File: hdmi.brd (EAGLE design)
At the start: 160 x 100 mm, 151 parts, among them IC1 FT2232HQ, U0 6SLX45CSG324, U1 MT41J64M16, U2 TPD12S016RKTR, U3 TPD12S016RKTR, U4 TPD12S016RKTR, U5 MNR18, U6 MNR18, U8 20Mhz

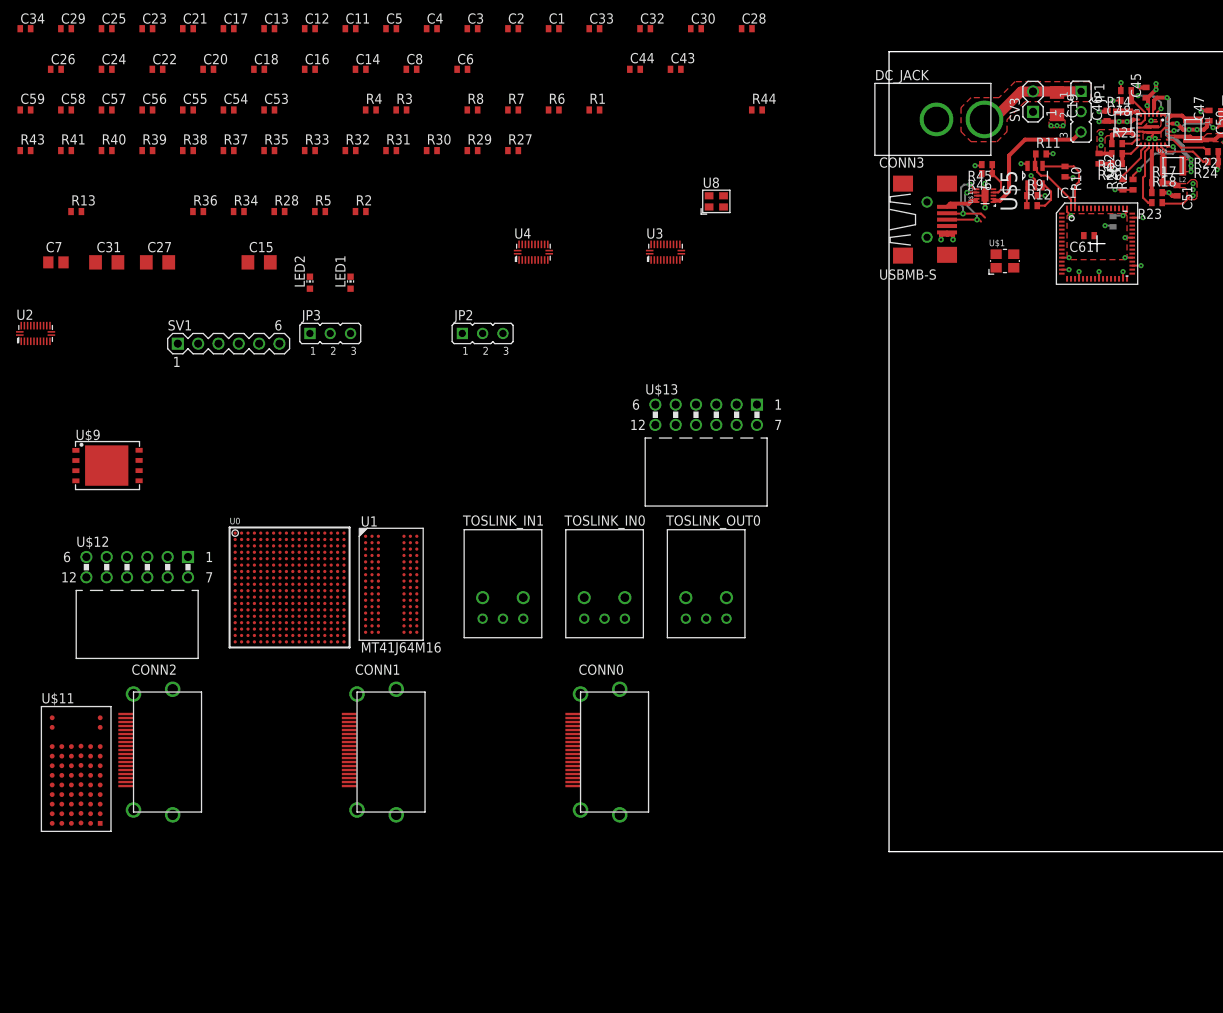
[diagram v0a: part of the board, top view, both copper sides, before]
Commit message: Rerouted USB, added more bypass capacitors at the FT2232H
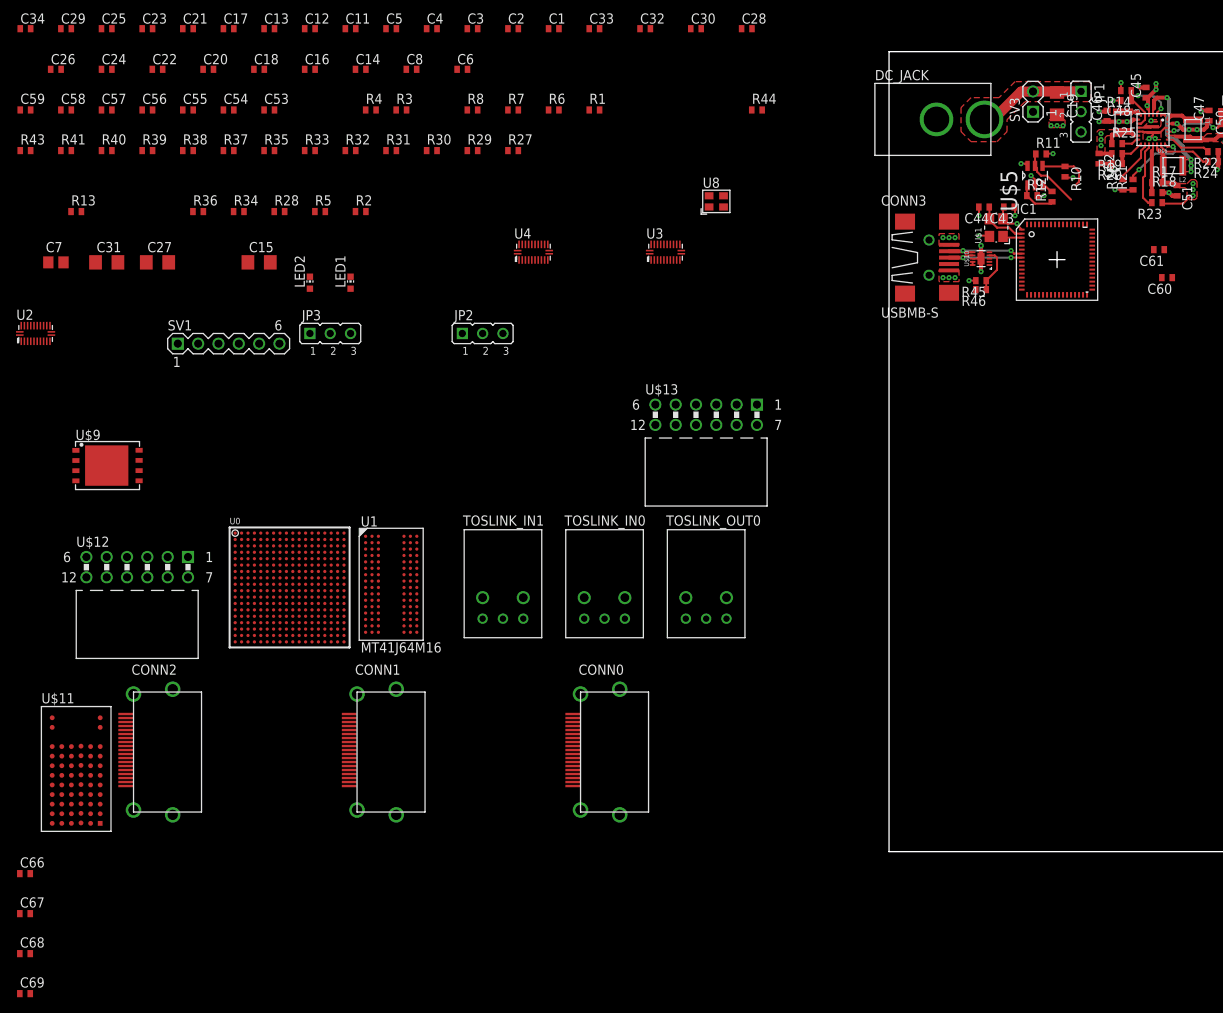
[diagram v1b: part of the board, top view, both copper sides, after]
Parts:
- added C66, C67, C68, C69: 0.1u, resistor:C0402
- C60: value 0.1u -> 4.7u
- moved C44 46.9 mm to (11.9, 80.6), turned to 180 degrees
- moved C43 45.1 mm to (15.0, 80.6), turned to 180 degrees
- moved R45 14.5 mm to (11.5, 71.4)
- moved R46 14.5 mm to (11.5, 70.2)
- moved C60 9.72 mm to (34.8, 71.8), flipped to the top, turned to 180 degrees
- moved C61 8.92 mm to (33.8, 75.2)
- moved U$10 7.89 mm to (11.5, 74.1)
- moved IC1 5.39 mm to (21.0, 74.0)
- moved CONN3 4.76 mm to (5.00, 74.2)
- moved U$1 4.35 mm to (13.4, 78.0), turned to 90 degrees
- moved R12 2.74 mm to (20.4, 81.9), turned to 90 degrees
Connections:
- net +1V8: now also C66.1, C67.1
- net +3V3: now also C68.1, C69.1
- net GND: now also C66.2, C67.2, C68.2, C69.2
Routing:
- net USB_VBUS: track 17.6 -> 0.00 mm
- net N$1: track 0.00 -> 6.39 mm
- net +1V8: track 5.31 -> 0.00 mm, vias 4 -> 0
- net N$45: track 4.51 -> 0.40 mm, vias 0 -> 3
- net N$5: track 0.00 -> 3.53 mm, vias 0 -> 1
- net N$10: track 4.42 -> 1.50 mm
- net +3V3: track 18.4 -> 15.5 mm, vias 12 -> 9
- net N$9: track 9.67 -> 6.82 mm
- net N$12: track 2.57 -> 5.03 mm
- net GND: track 36.7 -> 35.5 mm, vias 23 -> 22
- net N$6: track 9.15 -> 8.05 mm
- net USB_5V_ACK#: track 4.68 -> 5.62 mm
- net N$8: track 9.66 -> 10.4 mm
- added copper zone on layer 1, net N$45
- removed copper zone on layer 1, net +1V8

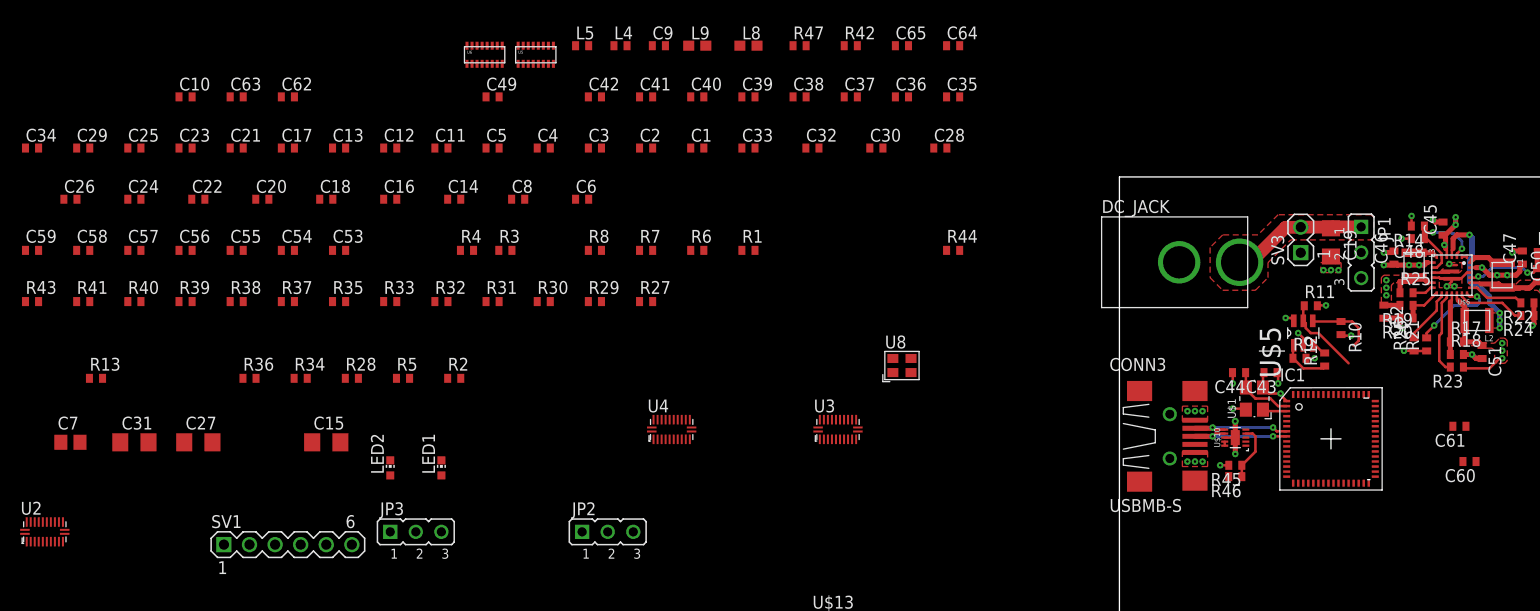
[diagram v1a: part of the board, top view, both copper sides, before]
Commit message: More USB related routing
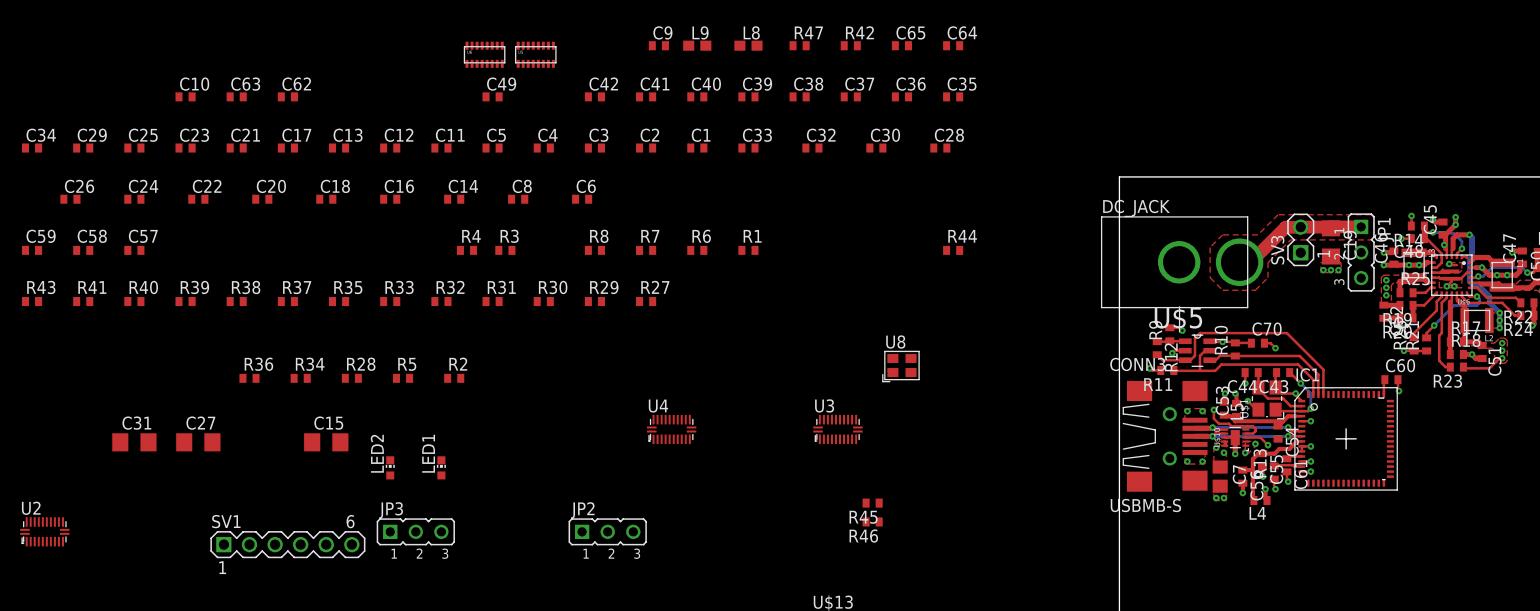
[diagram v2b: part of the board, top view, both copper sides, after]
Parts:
- added C70: 0.1u, resistor:C0402
- C53: value 0.1u -> 4.7u
- C54: value 4.7u -> 0.1u
- moved R13 117.3 mm to (15.4, 70.7), turned to 90 degrees
- moved C7 114.2 mm to (10.0, 70.2), turned to 270 degrees
- moved C56 107.3 mm to (12.2, 70.2), turned to 270 degrees
- moved C55 103.9 mm to (14.2, 71.9), turned to 270 degrees
- moved C54 99.9 mm to (15.8, 74.6), turned to 270 degrees
- moved C53 90.5 mm to (11.6, 76.9), turned to 90 degrees
- moved L4 77.9 mm to (14.0, 67.9), turned to 180 degrees
- moved L5 73.2 mm to (10.4, 77.0), turned to 270 degrees
- moved R46 36.3 mm to (-24.5, 65.8)
- moved R45 36.2 mm to (-24.5, 67.6)
- moved C61 17.6 mm to (16.6, 71.4), turned to 270 degrees
- moved R12 16.7 mm to (3.75, 83.0), turned to 270 degrees
- moved R11 15.6 mm to (4.75, 80.8), turned to 180 degrees
- moved R9 13.1 mm to (5.00, 84.4), turned to 90 degrees
- moved C60 11.2 mm to (27.0, 79.9), turned to 0 degrees
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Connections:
- net +3V3: now also C70.1
- net GND: now also C70.2
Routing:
- net N$10: track 1.50 -> 22.8 mm
- net N$6: track 8.05 -> 18.9 mm
- net N$31: track 0.00 -> 10.8 mm
- net GND: track 35.5 -> 44.8 mm, vias 22 -> 32
- net N$28: track 0.00 -> 9.00 mm
- net N$9: track 6.82 -> 13.7 mm
- net +3V3: track 15.5 -> 20.9 mm, vias 9 -> 10
- net N$5: track 3.53 -> 8.13 mm, vias 1 -> 2
- net +1V8: track 0.00 -> 3.08 mm
- net N$13: track 0.00 -> 2.82 mm
- net USB_5V_DISABLE: track 0.00 -> 2.51 mm, vias 0 -> 1
- net N$12: track 5.03 -> 2.83 mm
- net N$8: track 10.4 -> 11.9 mm
- net N$7: track 10.7 -> 12.2 mm
- net USB_5V_ACK#: track 5.62 -> 6.71 mm, vias 0 -> 1
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- added copper zone on layer 15, net N$45
- added copper zone on layer 1, net USB_VBUS
- added copper zone on layer 15, net USB_VBUS

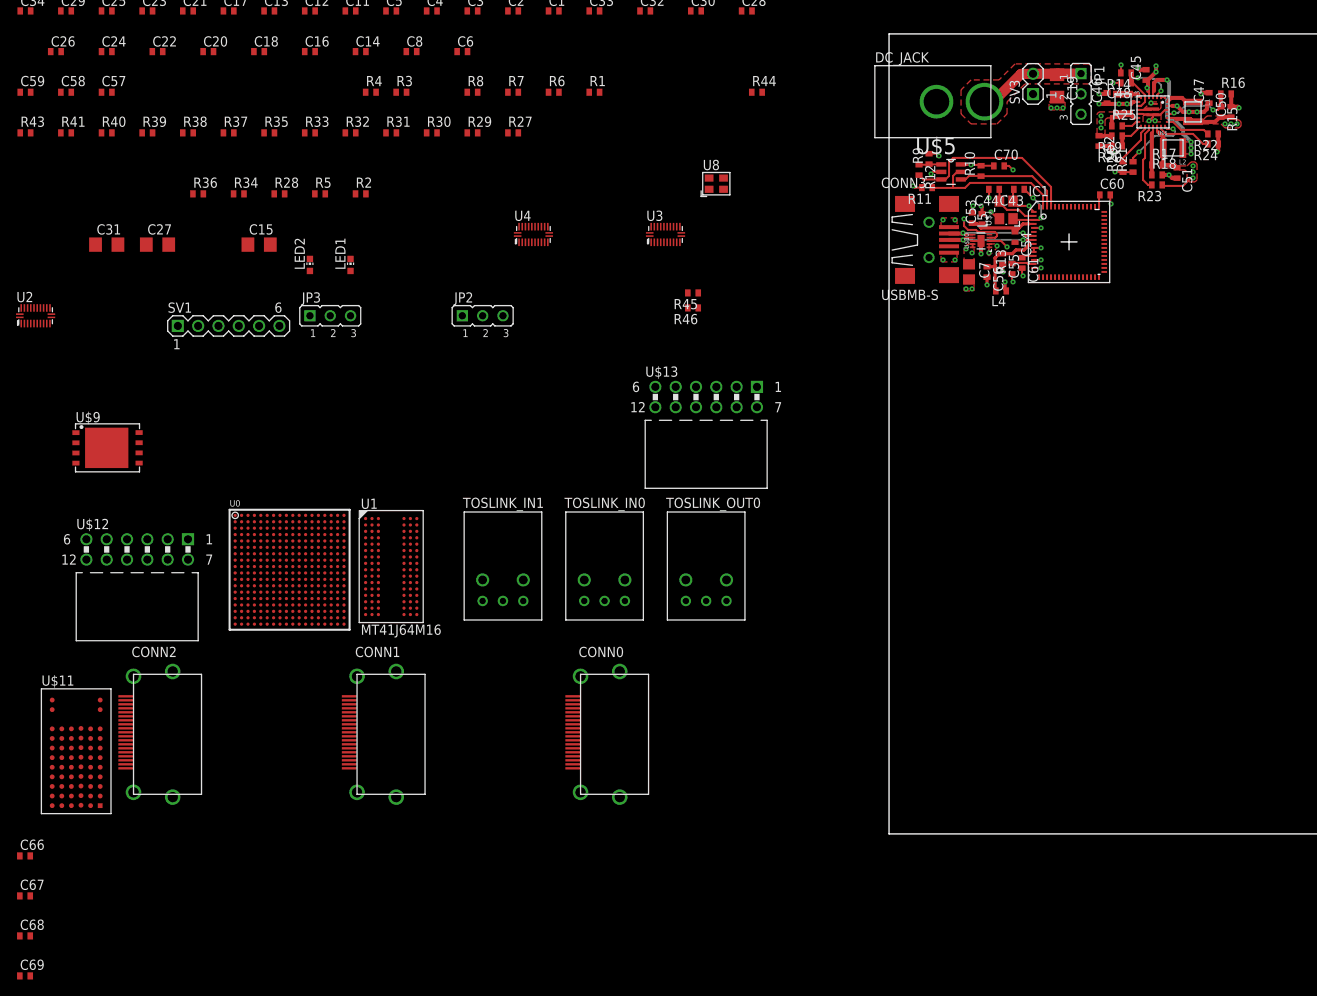
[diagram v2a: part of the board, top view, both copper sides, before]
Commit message: Changed FT2232H from package QFN to LQFP; Finished first routing of power management and USB
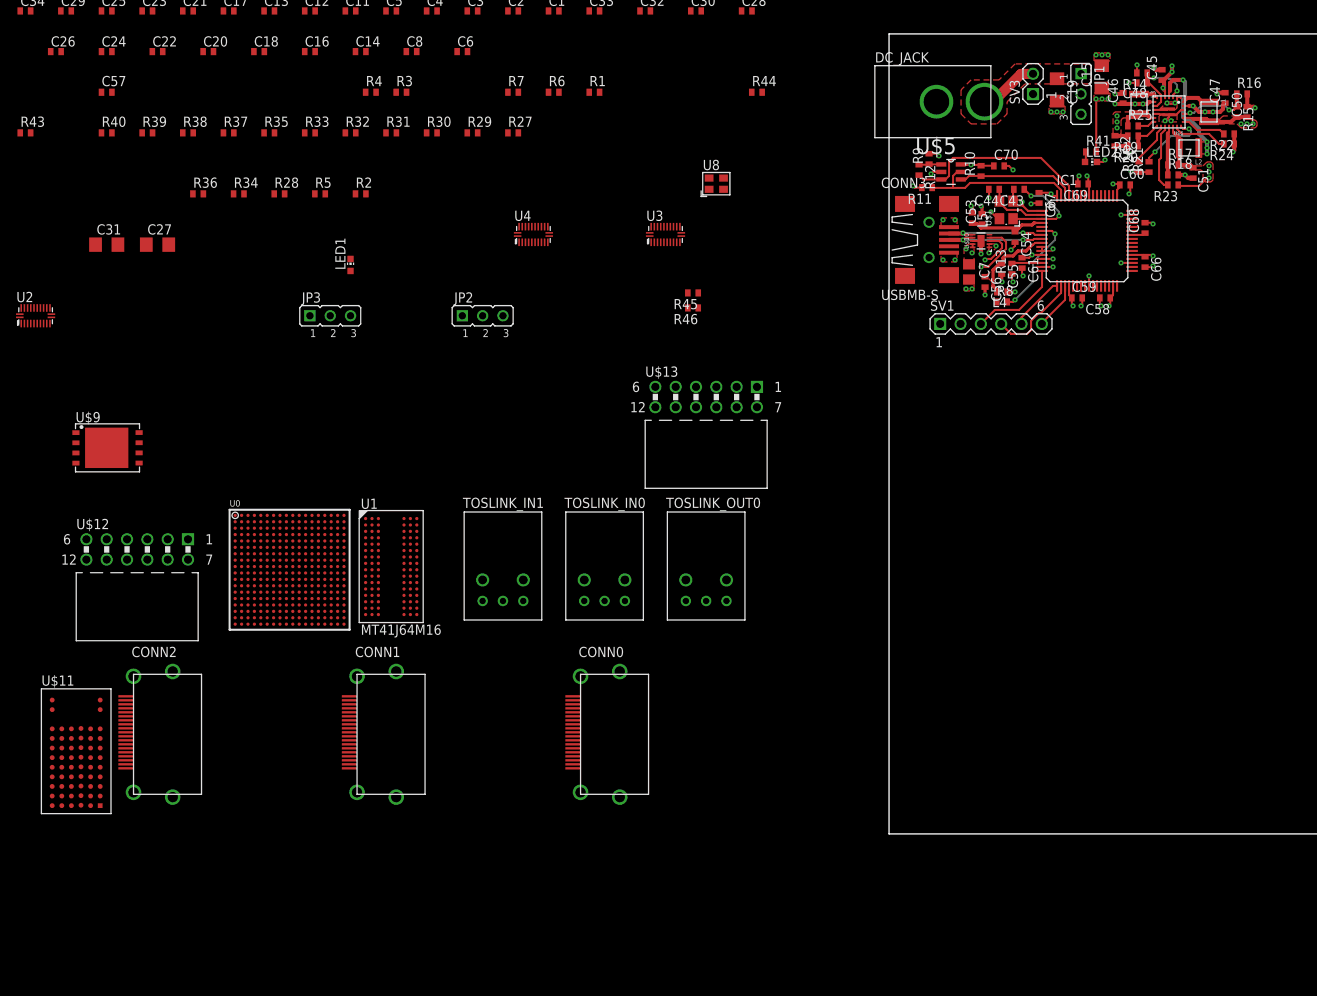
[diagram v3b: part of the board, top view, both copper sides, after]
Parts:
- IC1: value FT2232HQ -> FT2232HL; device prj-hdmi:QFN64 -> prj-hdmi:LQFP64
- moved C68 165.6 mm to (32.0, 75.8), turned to 90 degrees
- moved C69 165.2 mm to (24.2, 81.2), turned to 180 degrees
- moved C66 158.5 mm to (32.0, 71.5), turned to 270 degrees
- moved C67 153.9 mm to (18.8, 79.5), turned to 270 degrees
- moved C59 133.9 mm to (23.5, 67.0)
- moved C58 132.4 mm to (27.0, 67.0), turned to 180 degrees
- moved R41 128.1 mm to (25.2, 85.2)
- moved C15 107.4 mm to (26.6, 94.6), turned to 90 degrees
- moved LED2 98.5 mm to (25.2, 84.0), turned to 270 degrees
- moved SV1 95.3 mm to (12.8, 63.8)
- moved R8 71.2 mm to (14.1, 66.5)
- moved C60 2.80 mm to (29.5, 81.1)
- moved IC1 2.25 mm to (24.8, 74.1)
- moved C45 2.00 mm to (34.1, 94.9)
- moved C46 2.00 mm to (29.2, 92.0)
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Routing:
- net N$11: track 0.00 -> 13.2 mm, vias 0 -> 2
- net USB_TDO: track 0.00 -> 11.7 mm
- net USB_TCK: track 0.00 -> 11.6 mm
- net GND: track 44.8 -> 56.2 mm, vias 32 -> 46
- net +3V3: track 20.9 -> 30.5 mm, vias 10 -> 13
- net +1V8: track 3.08 -> 10.5 mm, vias 0 -> 4
- net USB_TDI: track 0.00 -> 6.88 mm
- net +5V: track 20.5 -> 27.3 mm, vias 11 -> 14
- net CENTER: track 13.6 -> 7.52 mm
- net USB_TMS: track 0.00 -> 5.95 mm
- net N$5: track 8.13 -> 12.0 mm
- net USB_5V_DISABLE: track 2.51 -> 4.98 mm
- net N$47: track 0.00 -> 1.29 mm
- net N$6: track 18.9 -> 20.2 mm
- net N$28: track 9.00 -> 10.2 mm
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- added copper zone on layer 15, net +1V8
- added copper zone on layer 1, net +5V
- added copper zone on layer 1, net N$31

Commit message: Moved chips to their general direction
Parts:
- U5, U6: device resistor-net:MNR18 -> prj-hdmi:MNR18
- moved U$11 261.4 mm to (155.0, 60.0), turned to 270 degrees
- moved U$12 202.8 mm to (101.5, 89.5), turned to 180 degrees
- moved CONN1 183.0 mm to (110.5, 69.5)
- moved U$9 182.9 mm to (85.0, 53.0)
- moved U6 171.7 mm to (102.0, 72.0), turned to 270 degrees
- moved U2 162.4 mm to (54.1, 87.1)
- moved TOSLINK_IN1 157.6 mm to (108.0, 52.0), turned to 270 degrees
- moved U0 154.5 mm to (75.2, 69.6)
- moved U$13 147.5 mm to (120.5, 89.5), turned to 180 degrees
- moved CONN2 145.1 mm to (53.0, 27.0), turned to 270 degrees
- moved TOSLINK_IN0 129.7 mm to (78.5, 93.5), turned to 180 degrees
- moved R32 128.7 mm to (61.4, 90.7), turned to 90 degrees
- moved U3 124.5 mm to (96.5, 70.0), turned to 270 degrees
- moved CONN0 123.3 mm to (55.8, 95.5), turned to 90 degrees
- moved U5 117.2 mm to (54.0, 84.5), flipped to the bottom, turned to 180 degrees
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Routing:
- net GND: track 56.2 -> 74.3 mm, vias 46 -> 70
- net +3V3: track 30.5 -> 37.3 mm, vias 13 -> 25
- net +1V2: track 8.52 -> 14.8 mm, vias 3 -> 14
- net HDMI_RX0_DATA2_P: track 0.00 -> 3.90 mm
- net HDMI_RX0_CLK_P: track 0.00 -> 3.71 mm
- net HDMI_RX0_DATA0_N: track 0.00 -> 3.67 mm
- net HDMI_RX0_DATA2_N: track 0.00 -> 3.65 mm
- net HDMI_RX0_DATA1_P: track 0.00 -> 3.61 mm
- net HDMI_RX0_DATA1_N: track 0.00 -> 3.56 mm
- net HDMI_RX0_DATA0_P: track 0.00 -> 3.52 mm
- net N$50: track 0.00 -> 1.21 mm
- net HDMI_TX0_CEC_3V3: track 0.00 -> 0.57 mm, vias 0 -> 1
- net DDR3_CKE: track 0.00 -> 0.57 mm, vias 0 -> 1
- net DDR3_A0: track 0.00 -> 0.57 mm, vias 0 -> 1
- net BT_RESET#: track 0.00 -> 0.57 mm, vias 0 -> 1
